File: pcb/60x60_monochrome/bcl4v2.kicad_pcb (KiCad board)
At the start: 2 copper layers, 60 x 60 mm, 55 parts, among them J1 Conn_01x05, J10 Conn_01x01_Female, J11 Conn_01x01_Female, J12 Conn_01x01_Female, J13 Conn_01x01_Female, J14 Conn_01x02, J15 Conn_01x04, J2 Conn_01x05, J3 USB_OTG, J4 Conn_01x05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

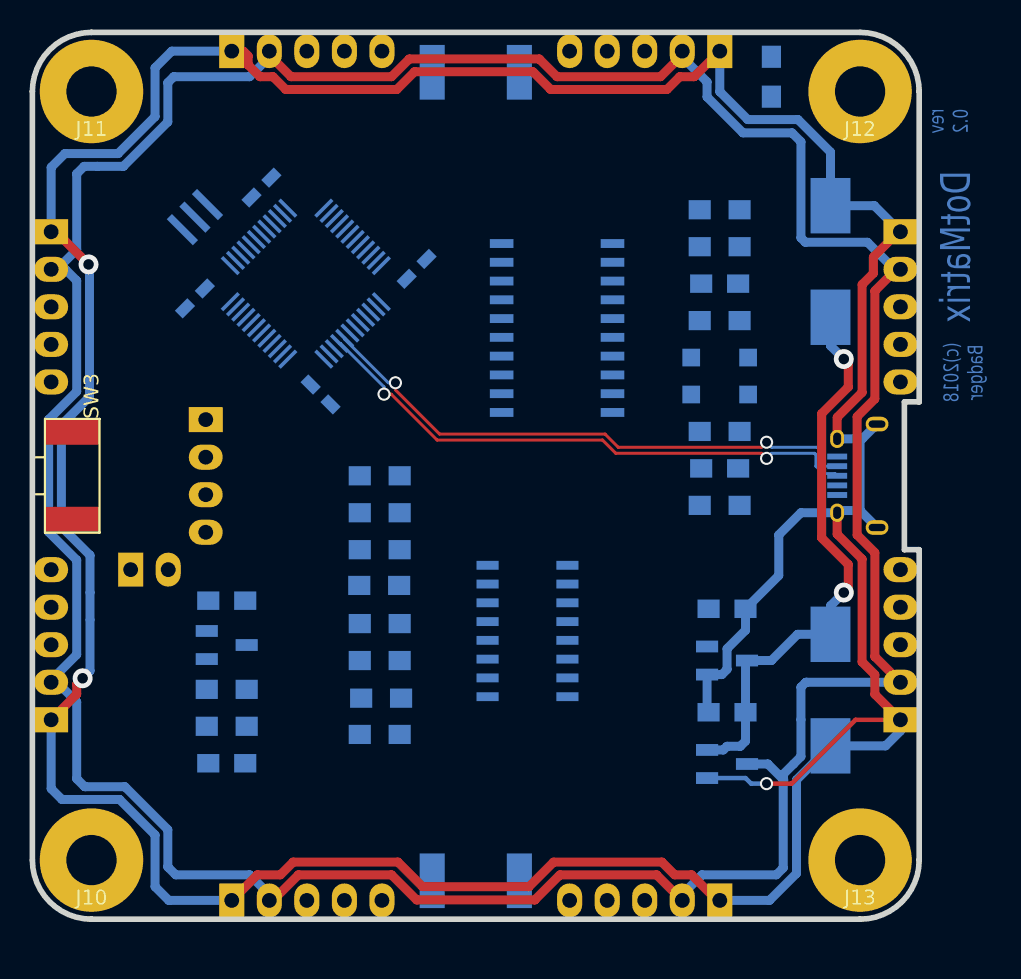
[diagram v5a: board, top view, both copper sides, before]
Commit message: - little bit more componnent shifting to ease soldering
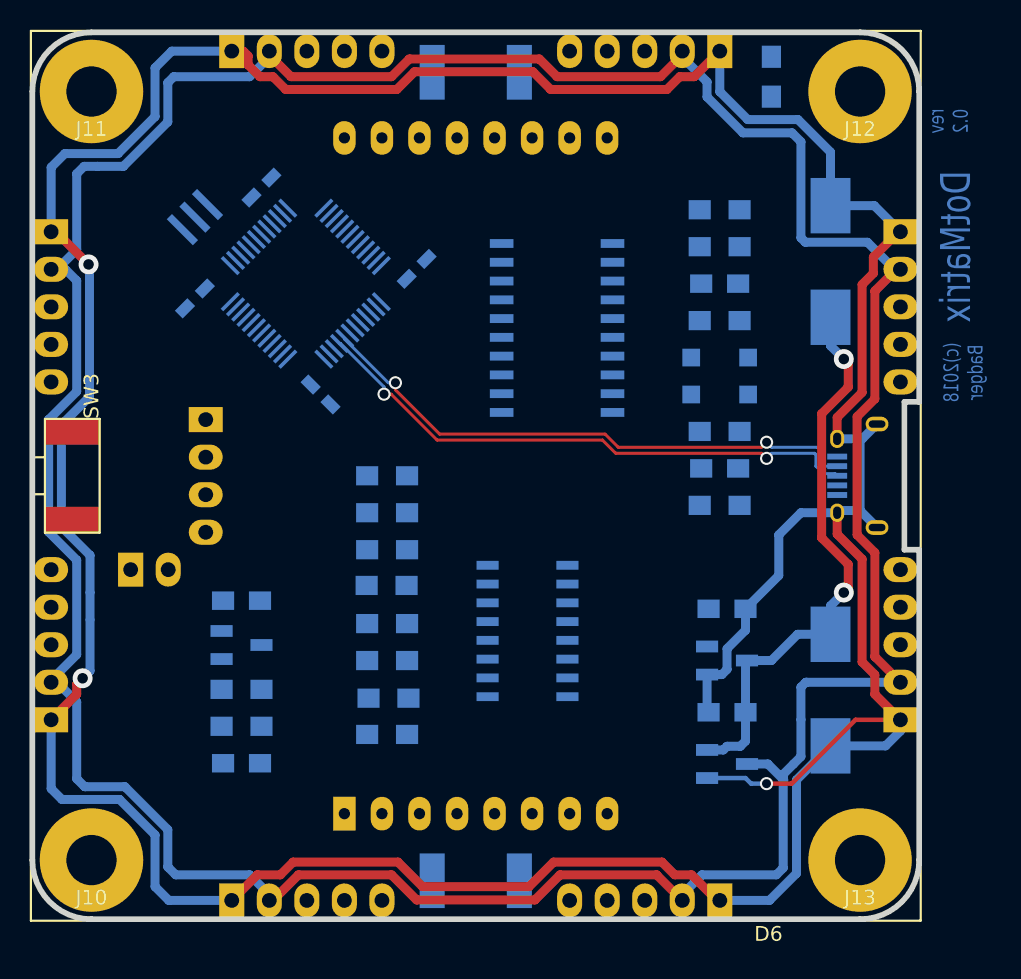
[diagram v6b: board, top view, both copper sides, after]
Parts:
- added D6: LED_MATRIX_8x8, kicad_libraries_new:badger_LED_MATRIX_8x8_60.2mmx60.2mm, F.Cu at (100.0, 100.0)
- moved C10 1.00 mm to (84.2, 119.5)
- moved C11 1.00 mm to (84.2, 108.5)
- moved Q1 1.00 mm to (84.2, 111.5)
- moved R13 1.00 mm to (84.2, 114.5)
- moved R16 1.00 mm to (84.2, 117.0)
- moved R10 0.50 mm to (94.0, 107.4)
- moved R11 0.50 mm to (94.0, 105.0)
- moved R12 0.50 mm to (94.0, 102.5)
- moved R3 0.50 mm to (94.0, 100.0)
- moved R6 0.50 mm to (94.0, 117.5)
- moved R7 0.50 mm to (94.1, 115.0)
- moved R8 0.50 mm to (94.0, 112.5)
- moved R9 0.50 mm to (94.0, 110.0)
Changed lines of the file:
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@@
   (general
     (links 160)
-    (no_connects 132)
+    (no_connects 130)
     (area 69.809499 69.809499 130.190501 130.190501)
     (thickness 1.6002)
@@
     (tracks 262)
     (zones 0)
-    (modules 55)
+    (modules 56)
     (nets 69)
   )
@@
   )
   (module Resistors_SMD:R_0805_HandSoldering (layer Back)
-    (at 93.5 117.5)
+    (at 94 117.5)
     (descr "Resistor SMD 0805, hand soldering")
     (tags "resistor 0805")
@@
   )
   (module Resistors_SMD:R_0805_HandSoldering (layer Back)
-    (at 93.594 115.046)
+    (at 94.094 115.046)
     (descr "Resistor SMD 0805, hand soldering")
     (tags "resistor 0805")
@@
   )
   (module Resistors_SMD:R_0805_HandSoldering (layer Back)
-    (at 93.5 112.5)
+    (at 94 112.5)
     (descr "Resistor SMD 0805, hand soldering")
     (tags "resistor 0805")
@@
   )
   (module Resistors_SMD:R_0805_HandSoldering (layer Back)
-    (at 93.5 110)
+    (at 94 110)
     (descr "Resistor SMD 0805, hand soldering")
     (tags "resistor 0805")
@@
   )
   (module Resistors_SMD:R_0805_HandSoldering (layer Back)
-    (at 93.466 107.419)
+    (at 93.966 107.419)
     (descr "Resistor SMD 0805, hand soldering")
     (tags "resistor 0805")
@@
   )
   (module Resistors_SMD:R_0805_HandSoldering (layer Back)
-    (at 93.5 105)
+    (at 94 105)
     (descr "Resistor SMD 0805, hand soldering")
     (tags "resistor 0805")
@@
   )
   (module Resistors_SMD:R_0805_HandSoldering (layer Back)
-    (at 93.5 102.5)
+    (at 94 102.5)
     (descr "Resistor SMD 0805, hand soldering")
     (tags "resistor 0805")
@@
   )
   (module Resistors_SMD:R_0805_HandSoldering (layer Back)
-    (at 83.15 114.45 180)
+    (at 84.15 114.45 180)
     (descr "Resistor SMD 0805, hand soldering")
     (tags "resistor 0805")
@@
   )
   (module Capacitors_SMD:C_0805_HandSoldering (layer Back)
-    (at 83.15 119.45 180)
+    (at 84.15 119.45 180)
     (descr "Capacitor SMD 0805, hand soldering")
     (tags "capacitor 0805")
@@
   )
   (module Capacitors_SMD:C_0805_HandSoldering (layer Back)
-    (at 83.15 108.45 180)
+    (at 84.15 108.45 180)
     (descr "Capacitor SMD 0805, hand soldering")
     (tags "capacitor 0805")
@@
   )
   (module Resistors_SMD:R_0805_HandSoldering (layer Back)
-    (at 93.5 100)
+    (at 94 100)
     (descr "Resistor SMD 0805, hand soldering")
     (tags "resistor 0805")
@@
   )
   (module Resistors_SMD:R_0805_HandSoldering (layer Back)
-    (at 83.15 116.95 180)
+    (at 84.15 116.95 180)
     (descr "Resistor SMD 0805, hand soldering")
     (tags "resistor 0805")
@@
   )
   (module kicad_libraries_new:badger_SOT-23_handsolder (layer Back)
-    (at 83.15 111.45)
+    (at 84.15 111.45)
     (descr "SOT-23, Standard")
     (tags SOT-23)
@@
     )
   )
+  (module kicad_libraries_new:badger_LED_MATRIX_8x8_60.2mmx60.2mm (layer Front)
+    (at 100 100)
+    (fp_text reference D6 (at 19.8 31) (layer F.SilkS)
+      (effects (font (size 1 1) (thickness 0.15)))
+    )
+    (fp_text value LED_MATRIX_8x8 (at 0 -31) (layer F.Fab)
+      (effects (font (size 1 1) (thickness 0.15)))
+    )
+    (fp_line (start -30.1 -30.1) (end 30.1 -30.1) (layer F.SilkS) (width 0.15))
+    (fp_line (start 30.1 -30.1) (end 30.1 30.1) (layer F.SilkS) (width 0.15))
+    (fp_line (start 30.1 30.1) (end -30.1 30.1) (layer F.SilkS) (width 0.15))
+    (fp_line (start -30.1 30.1) (end -30.1 -30.1) (layer F.SilkS) (width 0.15))
+    (pad 16 thru_hole oval (at -8.89 -22.86) (size 1.524 2.286) (drill 0.762) (layers *.Cu *.Mask)
+      (net 17 /LED_matrix/OUT_C8))
+    (pad 15 thru_hole oval (at -6.35 -22.86) (size 1.524 2.286) (drill 0.762) (layers *.Cu *.Mask)
+      (net 18 /LED_matrix/OUT_C7))
+    (pad 14 thru_hole oval (at -3.81 -22.86) (size 1.524 2.286) (drill 0.762) (layers *.Cu *.Mask)
+      (net 19 /LED_matrix/OUT_A1))
+    (pad 13 thru_hole oval (at -1.27 -22.86) (size 1.524 2.286) (drill 0.762) (layers *.Cu *.Mask)
+      (net 20 /LED_matrix/OUT_C1))
+    (pad 12 thru_hole oval (at 1.27 -22.86) (size 1.524 2.286) (drill 0.762) (layers *.Cu *.Mask)
+      (net 21 /LED_matrix/OUT_A3))
+    (pad 11 thru_hole oval (at 3.81 -22.86) (size 1.524 2.286) (drill 0.762) (layers *.Cu *.Mask)
+      (net 22 /LED_matrix/OUT_C6))
+    (pad 10 thru_hole oval (at 6.35 -22.86) (size 1.524 2.286) (drill 0.762) (layers *.Cu *.Mask)
+      (net 23 /LED_matrix/OUT_C4))
+    (pad 9 thru_hole oval (at 8.89 -22.86) (size 1.524 2.286) (drill 0.762) (layers *.Cu *.Mask)
+      (net 24 /LED_matrix/OUT_A0))
+    (pad 7 thru_hole oval (at 6.35 22.86) (size 1.524 2.286) (drill 0.762) (layers *.Cu *.Mask)
+      (net 25 /LED_matrix/OUT_A5))
+    (pad 8 thru_hole oval (at 8.89 22.86) (size 1.524 2.286) (drill 0.762) (layers *.Cu *.Mask)
+      (net 26 /LED_matrix/OUT_A2))
+    (pad 4 thru_hole oval (at -1.27 22.86) (size 1.524 2.286) (drill 0.762) (layers *.Cu *.Mask)
+      (net 27 /LED_matrix/OUT_C3))
+    (pad 5 thru_hole oval (at 1.27 22.86) (size 1.524 2.286) (drill 0.762) (layers *.Cu *.Mask)
+      (net 28 /LED_matrix/OUT_A7))
+    (pad 3 thru_hole oval (at -3.81 22.86) (size 1.524 2.286) (drill 0.762) (layers *.Cu *.Mask)
+      (net 29 /LED_matrix/OUT_C2))
+    (pad 6 thru_hole oval (at 3.81 22.86) (size 1.524 2.286) (drill 0.762) (layers *.Cu *.Mask)
+      (net 30 /LED_matrix/OUT_C5))
+    (pad 2 thru_hole oval (at -6.35 22.86) (size 1.524 2.286) (drill 0.762) (layers *.Cu *.Mask)
+      (net 31 /LED_matrix/OUT_A6))
+    (pad 1 thru_hole rect (at -8.89 22.86) (size 1.524 2.286) (drill 0.762) (layers *.Cu *.Mask)
+      (net 32 /LED_matrix/OUT_A4))
+  )
   (dimension 7.3 (width 0.3048) (layer Cmts.User)

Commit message: - fix unroutable corner
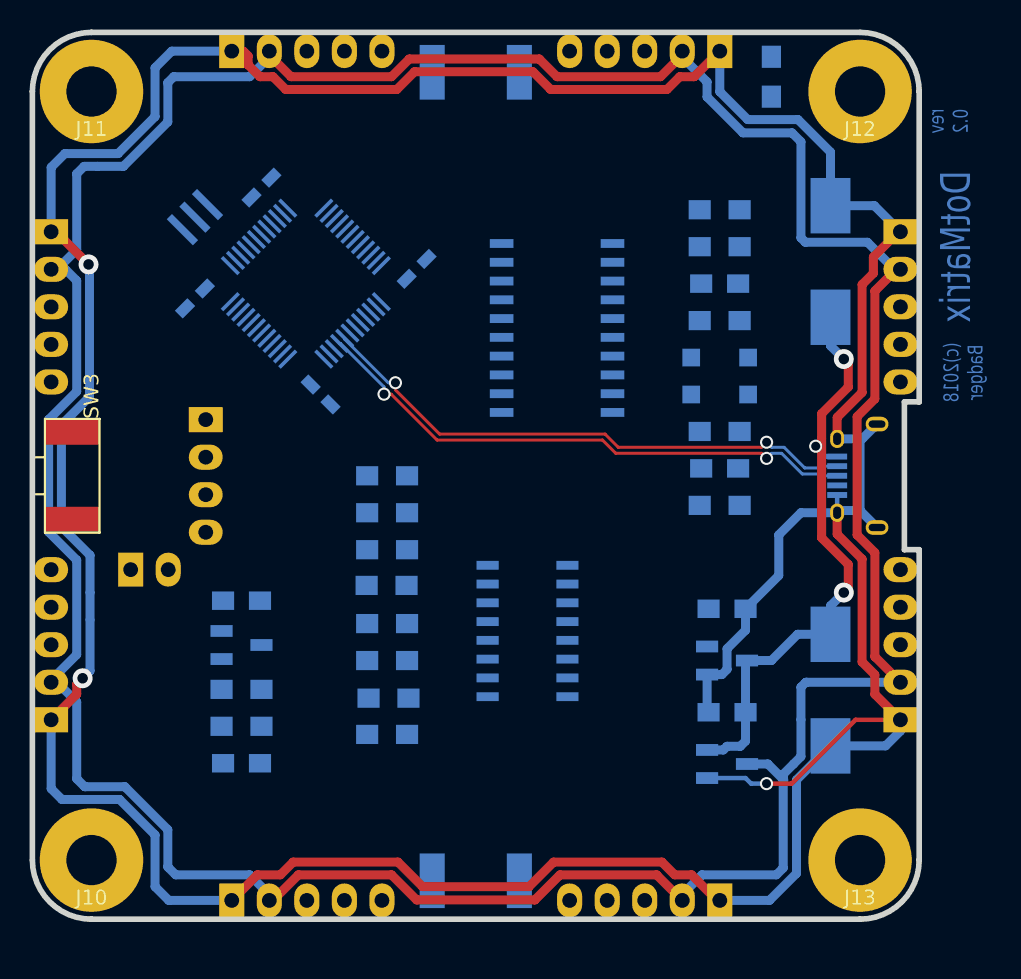
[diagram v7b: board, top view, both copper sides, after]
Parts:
- removed D6: LED_MATRIX_8x8, kicad_libraries_new:badger_LED_MATRIX_8x8_60.2mmx60.2mm
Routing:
- net +5V: track 39.6 -> 42.6 mm, vias 2 -> 3
- net GND: track 274.0 -> 275.2 mm

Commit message: -add missing LCD component footprint
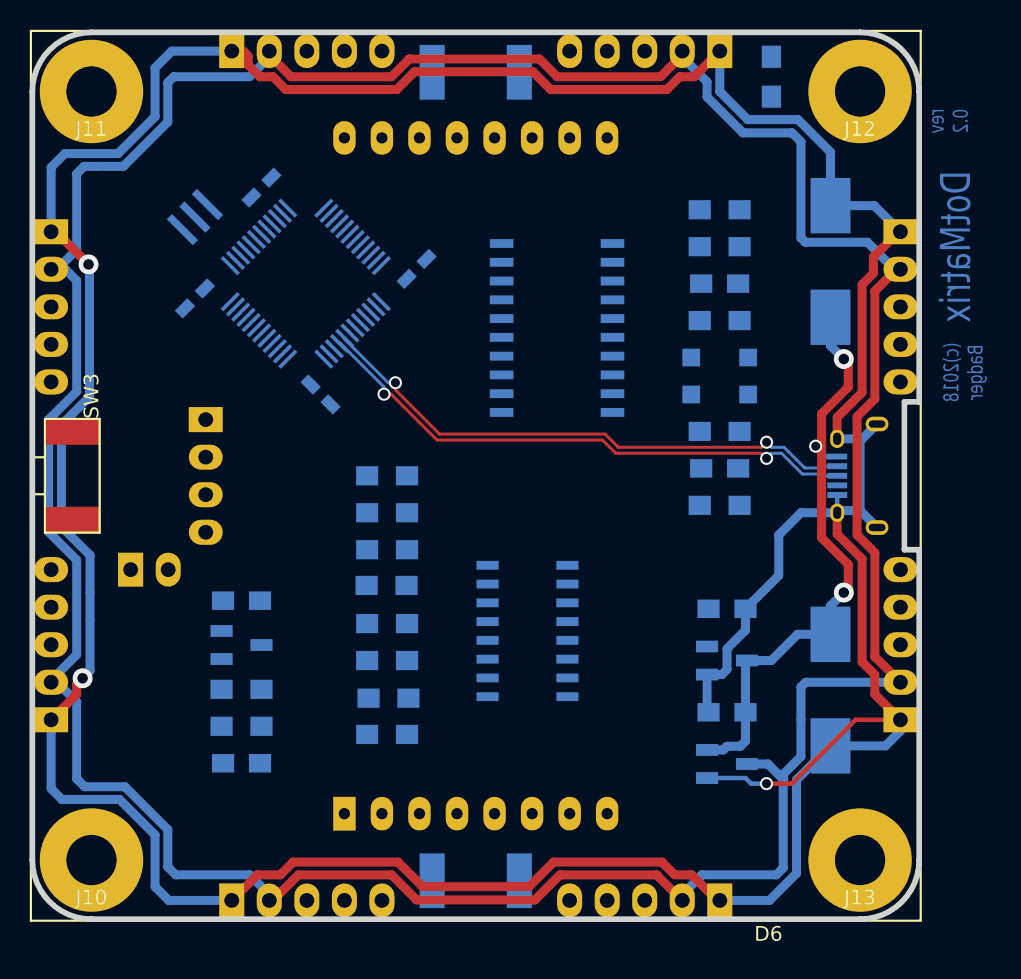
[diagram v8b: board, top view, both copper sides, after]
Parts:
- added D6: LED_MATRIX_8x8, kicad_libraries_new:badger_LED_MATRIX_8x8_60.2mmx60.2mm, F.Cu at (100.0, 100.0)
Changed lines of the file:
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@@
 (kicad_pcb (version 4) (host pcbnew 4.0.7-e2-6376~58~ubuntu16.04.1)
   (general
-    (links 144)
-    (no_connects 112)
+    (links 160)
+    (no_connects 128)
     (area 69.809499 69.809499 130.190501 130.190501)
     (thickness 1.6002)
@@
     (tracks 269)
     (zones 0)
-    (modules 55)
+    (modules 56)
     (nets 69)
   )
@@
     )
   )
+  (module kicad_libraries_new:badger_LED_MATRIX_8x8_60.2mmx60.2mm (layer Front)
+    (at 100 100)
+    (fp_text reference D6 (at 19.8 31) (layer F.SilkS)
+      (effects (font (size 1 1) (thickness 0.15)))
+    )
+    (fp_text value LED_MATRIX_8x8 (at 0 -31) (layer F.Fab)
+      (effects (font (size 1 1) (thickness 0.15)))
+    )
+    (fp_line (start -30.1 -30.1) (end 30.1 -30.1) (layer F.SilkS) (width 0.15))
+    (fp_line (start 30.1 -30.1) (end 30.1 30.1) (layer F.SilkS) (width 0.15))
+    (fp_line (start 30.1 30.1) (end -30.1 30.1) (layer F.SilkS) (width 0.15))
+    (fp_line (start -30.1 30.1) (end -30.1 -30.1) (layer F.SilkS) (width 0.15))
+    (pad 16 thru_hole oval (at -8.89 -22.86) (size 1.524 2.286) (drill 0.762) (layers *.Cu *.Mask)
+      (net 17 /LED_matrix/OUT_C8))
+    (pad 15 thru_hole oval (at -6.35 -22.86) (size 1.524 2.286) (drill 0.762) (layers *.Cu *.Mask)
+      (net 18 /LED_matrix/OUT_C7))
+    (pad 14 thru_hole oval (at -3.81 -22.86) (size 1.524 2.286) (drill 0.762) (layers *.Cu *.Mask)
+      (net 19 /LED_matrix/OUT_A1))
+    (pad 13 thru_hole oval (at -1.27 -22.86) (size 1.524 2.286) (drill 0.762) (layers *.Cu *.Mask)
+      (net 20 /LED_matrix/OUT_C1))
+    (pad 12 thru_hole oval (at 1.27 -22.86) (size 1.524 2.286) (drill 0.762) (layers *.Cu *.Mask)
+      (net 21 /LED_matrix/OUT_A3))
+    (pad 11 thru_hole oval (at 3.81 -22.86) (size 1.524 2.286) (drill 0.762) (layers *.Cu *.Mask)
+      (net 22 /LED_matrix/OUT_C6))
+    (pad 10 thru_hole oval (at 6.35 -22.86) (size 1.524 2.286) (drill 0.762) (layers *.Cu *.Mask)
+      (net 23 /LED_matrix/OUT_C4))
+    (pad 9 thru_hole oval (at 8.89 -22.86) (size 1.524 2.286) (drill 0.762) (layers *.Cu *.Mask)
+      (net 24 /LED_matrix/OUT_A0))
+    (pad 7 thru_hole oval (at 6.35 22.86) (size 1.524 2.286) (drill 0.762) (layers *.Cu *.Mask)
+      (net 25 /LED_matrix/OUT_A5))
+    (pad 8 thru_hole oval (at 8.89 22.86) (size 1.524 2.286) (drill 0.762) (layers *.Cu *.Mask)
+      (net 26 /LED_matrix/OUT_A2))
+    (pad 4 thru_hole oval (at -1.27 22.86) (size 1.524 2.286) (drill 0.762) (layers *.Cu *.Mask)
+      (net 27 /LED_matrix/OUT_C3))
+    (pad 5 thru_hole oval (at 1.27 22.86) (size 1.524 2.286) (drill 0.762) (layers *.Cu *.Mask)
+      (net 28 /LED_matrix/OUT_A7))
+    (pad 3 thru_hole oval (at -3.81 22.86) (size 1.524 2.286) (drill 0.762) (layers *.Cu *.Mask)
+      (net 29 /LED_matrix/OUT_C2))
+    (pad 6 thru_hole oval (at 3.81 22.86) (size 1.524 2.286) (drill 0.762) (layers *.Cu *.Mask)
+      (net 30 /LED_matrix/OUT_C5))
+    (pad 2 thru_hole oval (at -6.35 22.86) (size 1.524 2.286) (drill 0.762) (layers *.Cu *.Mask)
+      (net 31 /LED_matrix/OUT_A6))
+    (pad 1 thru_hole rect (at -8.89 22.86) (size 1.524 2.286) (drill 0.762) (layers *.Cu *.Mask)
+      (net 32 /LED_matrix/OUT_A4))
+  )
   (dimension 7.3 (width 0.3048) (layer Cmts.User)
     (gr_text "7,300 mm" (at 105.45 147.2256) (layer Cmts.User)
@@
     (arrow2b (pts (xy 100 96) (xy 101.126504 95.413579)))
   )
-  (segment (start 124.45 101.3) (end 124.45 102.5) (width 0.3048) (layer Back) (net 1) (status C00000))
+  (segment (start 124.45 101.3) (end 124.45 102.5) (width 0.3048) (layer Back) (net 1))
   (segment (start 121.371258 120.828742) (end 125.69 116.51) (width 0.3048) (layer Front) (net 1))
   (segment (start 125.69 116.51) (end 128.73 116.51) (width 0.3048) (layer Front) (net 1))
@@
   (segment (start 116.51 71.27) (end 116.51 71.49) (width 0.6096) (layer Front) (net 1))
   (segment (start 83.49 128.73) (end 83.23 128.73) (width 0.6096) (layer Back) (net 1))
-  (segment (start 124.45 98.7) (end 123.7 98.7) (width 0.3048) (layer Back) (net 4) (status 400000))
+  (segment (start 124.45 98.7) (end 123.7 98.7) (width 0.3048) (layer Back) (net 4))
   (segment (start 123.5 97.5) (end 123.4 97.5) (width 0.3048) (layer Front) (net 4))
   (segment (start 123.4 97.6) (end 123.5 97.5) (width 0.3048) (layer Front) (net 4))
